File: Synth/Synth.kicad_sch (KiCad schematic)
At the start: 13 parts, among them SW1 Reset, SW2 Boot, U1 ESP32-S2-SOLO, U11 LM321, U12 LM321, U2 LM321

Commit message: changed the potentiometer footprints
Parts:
- C10, C7, C8, C9: footprint (none) -> Capacitor_SMD:C_0805_2012Metric
- R1, R2, R3: footprint (none) -> Resistor_SMD:R_0805_2012Metric
- SW1: footprint (none) -> Button_Switch_SMD:SW_DIP_SPSTx01_Slide_6.7x4.1mm_W6.73mm_P2.54mm_LowProfile_JPin
- SW2: footprint (none) -> Button_Switch_THT:SW_PUSH_6mm_H7.3mm
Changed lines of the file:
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@@
       (effects (font (size 1.27 1.27)) (justify left))
     )
-    (property "Footprint" "" (at 194.6402 30.353 0)
+    (property "Footprint" "Capacitor_SMD:C_0805_2012Metric" (at 194.6402 30.353 0)
       (effects (font (size 1.27 1.27)) hide)
     )
@@
       (effects (font (size 1.27 1.27)) (justify left))
     )
-    (property "Footprint" "" (at 147.447 40.767 0)
+    (property "Footprint" "Resistor_SMD:R_0805_2012Metric" (at 147.447 40.767 0)
       (effects (font (size 1.27 1.27)) hide)
     )
@@
       (effects (font (size 1.27 1.27)))
     )
-    (property "Footprint" "" (at 255.143 71.7042 0)
+    (property "Footprint" "Capacitor_SMD:C_0805_2012Metric" (at 255.143 71.7042 0)
       (effects (font (size 1.27 1.27)) hide)
     )
@@
       (effects (font (size 1.27 1.27)))
     )
-    (property "Footprint" "" (at 138.049 37.846 0)
+    (property "Footprint" "Button_Switch_SMD:SW_DIP_SPSTx01_Slide_6.7x4.1mm_W6.73mm_P2.54mm_LowProfile_JPin" (at 138.049 37.846 0)
       (effects (font (size 1.27 1.27)) hide)
     )
@@
       (effects (font (size 1.27 1.27)))
     )
-    (property "Footprint" "" (at 272.288 85.344 0)
+    (property "Footprint" "Resistor_SMD:R_0805_2012Metric" (at 272.288 85.344 0)
       (effects (font (size 1.27 1.27)) hide)
     )
@@
       (effects (font (size 1.27 1.27)))
     )
-    (property "Footprint" "" (at 258.318 57.023 0)
+    (property "Footprint" "Button_Switch_THT:SW_PUSH_6mm_H7.3mm" (at 258.318 57.023 0)
       (effects (font (size 1.27 1.27)) hide)
     )
@@
       (effects (font (size 1.27 1.27)) (justify left))
     )
-    (property "Footprint" "" (at 255.397 89.535 0)
+    (property "Footprint" "Resistor_SMD:R_0805_2012Metric" (at 255.397 89.535 0)
       (effects (font (size 1.27 1.27)) hide)
     )
@@
       (effects (font (size 1.27 1.27)))
     )
-    (property "Footprint" "" (at 134.112 50.3682 0)
+    (property "Footprint" "Capacitor_SMD:C_0805_2012Metric" (at 134.112 50.3682 0)
       (effects (font (size 1.27 1.27)) hide)
     )
@@
       (effects (font (size 1.27 1.27)) (justify left))
     )
-    (property "Footprint" "" (at 202.6412 30.353 0)
-      (effects (font (size 1.27 1.27)) hide)
-    )
+    (property "Footprint" "Capacitor_SMD:C_0805_2012Metric" (at 202.6412 30.353 0)
+      (effects (font (size 1.27 1.27)) hide)
+    )

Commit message: almost done w layoutgit add *
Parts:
- added JP1+1: SolderJumper_2_Open, Jumper:SolderJumper-2_P1.3mm_Bridged_RoundedPad1.0x1.5mm, symbol Jumper:SolderJumper_2_Open
- added R4: 20k, Resistor_SMD:R_0805_2012Metric, symbol Device:R
- added RV1: 20k, Potentiometer_THT:Potentiometer_Bourns_3299W_Vertical, symbol Device:R_Potentiometer
- added TP1: TestPoint, TestPoint:TestPoint_Pad_2.5x2.5mm, symbol Connector:TestPoint
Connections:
- net GND: now also R4.2, TP1.1
- net V_out+: now also RV1.1
- new net: JP1+1.1 (A), RV1.2, RV1.3
- new net: JP1+1.2 (B), R4.1
- no-connect marks 0 -> 34

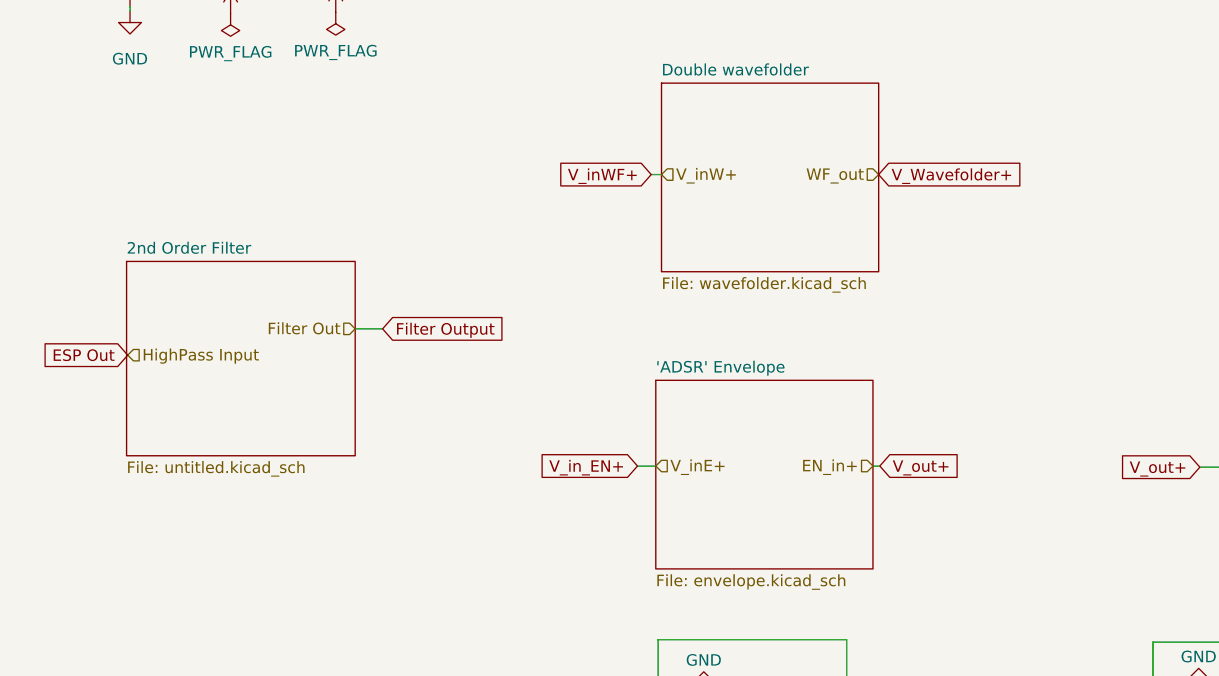
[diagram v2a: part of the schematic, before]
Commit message: changed hierarchical labels
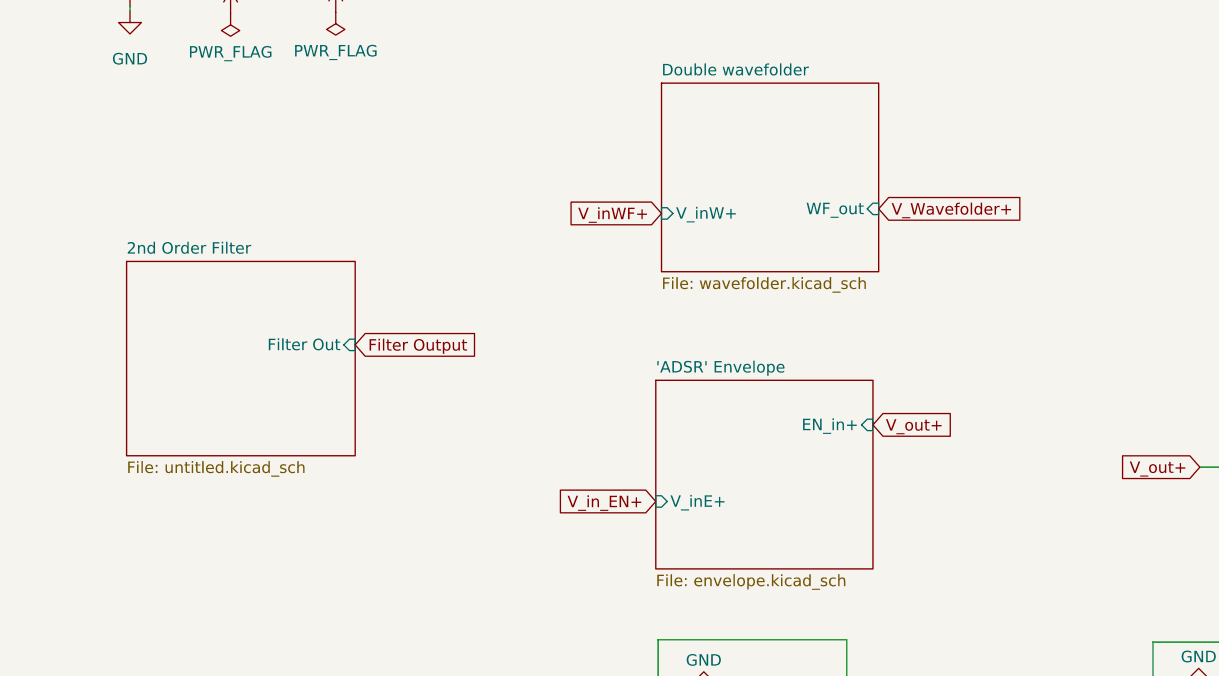
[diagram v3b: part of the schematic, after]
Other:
- sheet 'ADSR' Envelope ports: added EN_in+, V_inE+; removed none
- sheet 2nd Order Filter ports: added Filter Out; removed none
- sheet Double wavefolder ports: added V_inW+, WF_out; removed none
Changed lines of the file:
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@@
-    (stroke (width 0) (type default))
-  )
-  (wire (pts (xy 80.137 146.177) (xy 82.169 146.177))
     (stroke (width 0) (type default))
   )
@@
     (stroke (width 0) (type default))
   )
-  (wire (pts (xy 51.816 130.937) (xy 48.768 130.937))
-    (stroke (width 0) (type default))
-  )
   (wire (pts (xy 255.397 84.963) (xy 262.636 84.963))
     (stroke (width 0) (type default))
   )
-  (wire (pts (xy 81.661 113.792) (xy 82.804 113.792))
-    (stroke (width 0) (type default))
-  )
   (wire (pts (xy 103.378 179.197) (xy 104.648 179.197))
     (stroke (width 0) (type default))
   )
-  (wire (pts (xy 107.061 146.177) (xy 106.299 146.177))
-    (stroke (width 0) (type default))
-  )
   (wire (pts (xy 103.378 165.481) (xy 103.378 179.197))
     (stroke (width 0) (type default))
   )
-  (global_label "Filter Output" (shape input) (at 51.816 130.937 0) (fields_autoplaced)
-    (effects (font (size 1.27 1.27)) (justify left))
-    (property "Intersheetrefs" "${INTERSHEET_REFS}" (at 66.9568 130.937 0)
-      (effects (font (size 1.27 1.27)) (justify left) hide)
+  (global_label "V_inWF+" (shape input) (at 82.804 118.11 180) (fields_autoplaced)
+    (effects (font (size 1.27 1.27)) (justify right))
+    (property "Intersheetrefs" "${INTERSHEET_REFS}" (at 71.8964 118.11 0)
+      (effects (font (size 1.27 1.27)) (justify right) hide)
     )
   )
@@
     )
   )
-  (global_label "ESP Out" (shape input) (at 23.495 133.858 180) (fields_autoplaced)
-    (effects (font (size 1.27 1.27)) (justify right))
-    (property "Intersheetrefs" "${INTERSHEET_REFS}" (at 12.7085 133.858 0)
-      (effects (font (size 1.27 1.27)) (justify right) hide)
-    )
-  )
   (global_label "ESP Out" (shape input) (at 278.003 96.012 0) (fields_autoplaced)
     (effects (font (size 1.27 1.27)) (justify left))
@@
     )
   )
-  (global_label "V_Wavefolder+" (shape input) (at 106.934 113.792 0) (fields_autoplaced)
+  (global_label "V_Wavefolder+" (shape input) (at 106.934 117.602 0) (fields_autoplaced)
     (effects (font (size 1.27 1.27)) (justify left))
-    (property "Intersheetrefs" "${INTERSHEET_REFS}" (at 123.7681 113.792 0)
+    (property "Intersheetrefs" "${INTERSHEET_REFS}" (at 123.7681 117.602 0)
       (effects (font (size 1.27 1.27)) (justify left) hide)
     )
   )
-  (global_label "V_out+" (shape input) (at 107.061 146.177 0) (fields_autoplaced)
+  (global_label "Filter Output" (shape input) (at 48.768 132.715 0) (fields_autoplaced)
     (effects (font (size 1.27 1.27)) (justify left))
-    (property "Intersheetrefs" "${INTERSHEET_REFS}" (at 116.6985 146.177 0)
+    (property "Intersheetrefs" "${INTERSHEET_REFS}" (at 63.9088 132.715 0)
       (effects (font (size 1.27 1.27)) (justify left) hide)
     )
   )
-  (global_label "V_inWF+" (shape input) (at 81.661 113.792 180) (fields_autoplaced)
-    (effects (font (size 1.27 1.27)) (justify right))
-    (property "Intersheetrefs" "${INTERSHEET_REFS}" (at 70.7534 113.792 0)
-      (effects (font (size 1.27 1.27)) (justify right) hide)
+  (global_label "V_out+" (shape input) (at 106.299 141.605 0) (fields_autoplaced)
+    (effects (font (size 1.27 1.27)) (justify left))
+    (property "Intersheetrefs" "${INTERSHEET_REFS}" (at 115.9365 141.605 0)
+      (effects (font (size 1.27 1.27)) (justify left) hide)
     )
   )
@@
     )
   )
-  (global_label "V_in_EN+" (shape input) (at 80.137 146.177 180) (fields_autoplaced)
+  (global_label "V_in_EN+" (shape input) (at 82.169 150.114 180) (fields_autoplaced)
     (effects (font (size 1.27 1.27)) (justify right))
-    (property "Intersheetrefs" "${INTERSHEET_REFS}" (at 68.3223 146.177 0)
+    (property "Intersheetrefs" "${INTERSHEET_REFS}" (at 70.3543 150.114 0)
       (effects (font (size 1.27 1.27)) (justify right) hide)
     )
-  )
-  (hierarchical_label "WF_out" (shape input) (at 106.934 113.792 180) (fields_autoplaced)
-    (effects (font (size 1.27 1.27)) (justify right))
-  )
-  (hierarchical_label "V_inE+" (shape input) (at 82.169 146.177 0) (fields_autoplaced)
-    (effects (font (size 1.27 1.27)) (justify left))
-  )
-  (hierarchical_label "V_inW+" (shape input) (at 82.804 113.792 0) (fields_autoplaced)
-    (effects (font (size 1.27 1.27)) (justify left))
-  )
-  (hierarchical_label "HighPass Input" (shape input) (at 23.495 133.858 0) (fields_autoplaced)
-    (effects (font (size 1.27 1.27)) (justify left))
-  )
-  (hierarchical_label "EN_in+" (shape input) (at 106.299 146.177 180) (fields_autoplaced)
-    (effects (font (size 1.27 1.27)) (justify right))
-  )
-  (hierarchical_label "Filter Out" (shape input) (at 48.768 130.937 180) (fields_autoplaced)
-    (effects (font (size 1.27 1.27)) (justify right))
   )
   (symbol (lib_id "power:GND") (at 23.749 95.631 0) (unit 1)
@@
       (effects (font (size 1.27 1.27)) (justify left top))
     )
+    (pin "Filter Out" input (at 48.768 132.715 0)
+      (effects (font (size 1.27 1.27)) (justify right))
+    )
     (instances
       (project "Synth"
@@
       (effects (font (size 1.27 1.27)) (justify left top))
     )
+    (pin "EN_in+" input (at 106.299 141.605 0)
+      (effects (font (size 1.27 1.27)) (justify right))
+    )
+    (pin "V_inE+" input (at 82.169 150.114 180)
+      (effects (font (size 1.27 1.27)) (justify left))
+    )
     (instances
       (project "Synth"
@@
       (effects (font (size 1.27 1.27)) (justify left top))
     )
-    (instances
+    (pin "V_inW+" input (at 82.804 118.11 180)
+      (effects (font (size 1.27 1.27)) (justify left))
+    )
+    (pin "WF_out" input (at 106.934 117.602 0)
+      (effects (font (size 1.27 1.27)) (justify right))
+    )
+    (instances

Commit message: fixed
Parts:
- added TP2, TP3, TP4, TP5, TP6, TP7: TestPoint, TestPoint:TestPoint_Pad_2.5x2.5mm, symbol Connector:TestPoint
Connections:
- net +12V: now also TP7.1
- net +3.3V: now also TP6.1
- net Filter Output: now also TP2.1
- net V_Envelope+: now also TP5.1
- net V_Wavefolder+: now also TP4.1
- net V_out+: now also TP3.1
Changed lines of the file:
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@@
     (stroke (width 0) (type default))
+  )
+  (global_label "V_out+" (shape input) (at 64.77 75.311 90) (fields_autoplaced)
+    (effects (font (size 1.27 1.27)) (justify left))
+    (property "Intersheetrefs" "${INTERSHEET_REFS}" (at 64.77 65.6735 90)
+      (effects (font (size 1.27 1.27)) (justify left) hide)
+    )
   )
   (global_label "V_inWF+" (shape input) (at 82.804 118.11 180) (fields_autoplaced)
@@
     )
   )
+  (global_label "Filter Output" (shape input) (at 73.787 77.851 270) (fields_autoplaced)
+    (effects (font (size 1.27 1.27)) (justify right))
+    (property "Intersheetrefs" "${INTERSHEET_REFS}" (at 73.787 92.9918 90)
+      (effects (font (size 1.27 1.27)) (justify right) hide)
+    )
+  )
   (global_label "Filter Output" (shape input) (at 48.768 132.715 0) (fields_autoplaced)
     (effects (font (size 1.27 1.27)) (justify left))
@@
     )
   )
+  (global_label "V_Envelope+" (shape input) (at 64.77 57.15 90) (fields_autoplaced)
+    (effects (font (size 1.27 1.27)) (justify left))
+    (property "Intersheetrefs" "${INTERSHEET_REFS}" (at 64.77 42.1302 90)
+      (effects (font (size 1.27 1.27)) (justify left) hide)
+    )
+  )
   (global_label "V_out+" (shape input) (at 106.299 141.605 0) (fields_autoplaced)
     (effects (font (size 1.27 1.27)) (justify left))
@@
     )
   )
+  (global_label "V_Wavefolder+" (shape input) (at 73.406 57.658 90) (fields_autoplaced)
+    (effects (font (size 1.27 1.27)) (justify left))
+    (property "Intersheetrefs" "${INTERSHEET_REFS}" (at 73.406 40.8239 90)
+      (effects (font (size 1.27 1.27)) (justify left) hide)
+    )
+  )
   (global_label "V_in_EN+" (shape input) (at 82.169 150.114 180) (fields_autoplaced)
     (effects (font (size 1.27 1.27)) (justify right))
@@
         (path "/69caad27-d98a-4cdc-abd0-794bd5e6ba79"
           (reference "U2") (unit 1)
+        )
+      )
+    )
+  )
+  (symbol (lib_id "power:+3.3V") (at 88.138 67.056 0) (unit 1)
+    (in_bom yes) (on_board yes) (dnp no) (fields_autoplaced)
+    (property "Reference" "#PWR050" (at 88.138 70.866 0)
+      (effects (font (size 1.27 1.27)) hide)
+    )
+    (property "Value" "+3.3V" (at 88.138 62.357 0)
+      (effects (font (size 1.27 1.27)))
+    )
+    (property "Footprint" "" (at 88.138 67.056 0)
+      (effects (font (size 1.27 1.27)) hide)
+    )
+    (property "Datasheet" "" (at 88.138 67.056 0)
+      (effects (font (size 1.27 1.27)) hide)
+    )
+    (pin "1")
+    (instances
+      (project "Synth"
+        (path "/69caad27-d98a-4cdc-abd0-794bd5e6ba79"
+          (reference "#PWR050") (unit 1)
         )
       )
@@
     )
   )
+  (symbol (lib_id "Connector:TestPoint") (at 64.77 57.15 180) (unit 1)
+    (in_bom yes) (on_board yes) (dnp no) (fields_autoplaced)
+    (property "Reference" "TP5" (at 66.294 59.182 0)
+      (effects (font (size 1.27 1.27)) (justify right))
+    )
+    (property "Value" "TestPoint" (at 66.294 61.722 0)
+      (effects (font (size 1.27 1.27)) (justify right))
+    )
+    (property "Footprint" "TestPoint:TestPoint_Pad_2.5x2.5mm" (at 59.69 57.15 0)
+      (effects (font (size 1.27 1.27)) hide)
+    )
+    (property "Datasheet" "~" (at 59.69 57.15 0)
+      (effects (font (size 1.27 1.27)) hide)
+    )
+    (pin "1")
+    (instances
+      (project "Synth"
+        (path "/69caad27-d98a-4cdc-abd0-794bd5e6ba79"
+          (reference "TP5") (unit 1)
+        )
+      )
+    )
+  )
   (symbol (lib_id "power:GND") (at 87.503 171.577 180) (unit 1)
     (in_bom yes) (on_board yes) (dnp no)
@@
     )
   )
+  (symbol (lib_id "Connector:TestPoint") (at 73.406 57.658 180) (unit 1)
+    (in_bom yes) (on_board yes) (dnp no) (fields_autoplaced)
+    (property "Reference" "TP4" (at 74.93 59.69 0)
+      (effects (font (size 1.27 1.27)) (justify right))
+    )
+    (property "Value" "TestPoint" (at 74.93 62.23 0)
+      (effects (font (size 1.27 1.27)) (justify right))
+    )
+    (property "Footprint" "TestPoint:TestPoint_Pad_2.5x2.5mm" (at 68.326 57.658 0)
+      (effects (font (size 1.27 1.27)) hide)
+    )
+    (property "Datasheet" "~" (at 68.326 57.658 0)
+      (effects (font (size 1.27 1.27)) hide)
+    )
+    (pin "1")
+    (instances
+      (project "Synth"
+        (path "/69caad27-d98a-4cdc-abd0-794bd5e6ba79"
+          (reference "TP4") (unit 1)
+        )
+      )
+    )
+  )
   (symbol (lib_id "power:PWR_FLAG") (at 33.655 78.994 180) (unit 1)
     (in_bom yes) (on_board yes) (dnp no) (fields_autoplaced)
@@
         (path "/69caad27-d98a-4cdc-abd0-794bd5e6ba79"
           (reference "#PWR048") (unit 1)
+        )
+      )
+    )
+  )
+  (symbol (lib_id "Connector:TestPoint") (at 73.787 77.851 0) (unit 1)
+    (in_bom yes) (on_board yes) (dnp no) (fields_autoplaced)
+    (property "Reference" "TP2" (at 76.2 73.279 0)
+      (effects (font (size 1.27 1.27)) (justify left))
+    )
+    (property "Value" "TestPoint" (at 76.2 75.819 0)
+      (effects (font (size 1.27 1.27)) (justify left))
+    )
+    (property "Footprint" "TestPoint:TestPoint_Pad_2.5x2.5mm" (at 78.867 77.851 0)
+      (effects (font (size 1.27 1.27)) hide)
+    )
+    (property "Datasheet" "~" (at 78.867 77.851 0)
+      (effects (font (size 1.27 1.27)) hide)
+    )
+    (pin "1")
+    (instances
+      (project "Synth"
+        (path "/69caad27-d98a-4cdc-abd0-794bd5e6ba79"
+          (reference "TP2") (unit 1)
         )
       )
@@
     )
   )
+  (symbol (lib_id "power:+12V") (at 98.425 67.056 0) (unit 1)
+    (in_bom yes) (on_board yes) (dnp no)
+    (property "Reference" "#PWR051" (at 98.425 70.866 0)
+      (effects (font (size 1.27 1.27)) hide)
+    )
+    (property "Value" "+12V" (at 98.425 62.611 0)
+      (effects (font (size 1.27 1.27)))
+    )
+    (property "Footprint" "" (at 98.425 67.056 0)
+      (effects (font (size 1.27 1.27)) hide)
+    )
+    (property "Datasheet" "" (at 98.425 67.056 0)
+      (effects (font (size 1.27 1.27)) hide)
+    )
+    (pin "1")
+    (instances
+      (project "Synth"
+        (path "/69caad27-d98a-4cdc-abd0-794bd5e6ba79"
+          (reference "#PWR051") (unit 1)
+        )
+      )
+    )
+  )
   (symbol (lib_id "Device:R_Small") (at 147.447 40.767 0) (unit 1)
     (in_bom yes) (on_board yes) (dnp no) (fields_autoplaced)
@@
         (path "/69caad27-d98a-4cdc-abd0-794bd5e6ba79"
           (reference "R3") (unit 1)
+        )
+      )
+    )
+  )
+  (symbol (lib_id "Connector:TestPoint") (at 64.77 75.311 180) (unit 1)
+    (in_bom yes) (on_board yes) (dnp no) (fields_autoplaced)
+    (property "Reference" "TP3" (at 67.31 77.343 0)
+      (effects (font (size 1.27 1.27)) (justify right))
+    )
+    (property "Value" "TestPoint" (at 67.31 79.883 0)
+      (effects (font (size 1.27 1.27)) (justify right))
+    )
+    (property "Footprint" "TestPoint:TestPoint_Pad_2.5x2.5mm" (at 59.69 75.311 0)
+      (effects (font (size 1.27 1.27)) hide)
+    )
+    (property "Datasheet" "~" (at 59.69 75.311 0)
+      (effects (font (size 1.27 1.27)) hide)
+    )
+    (pin "1")
+    (instances
+      (project "Synth"
+        (path "/69caad27-d98a-4cdc-abd0-794bd5e6ba79"
+          (reference "TP3") (unit 1)
         )
       )
@@
     )
   )
+  (symbol (lib_id "Connector:TestPoint") (at 98.425 67.056 180) (unit 1)
+    (in_bom yes) (on_board yes) (dnp no) (fields_autoplaced)
+    (property "Reference" "TP7" (at 99.949 69.088 0)
+      (effects (font (size 1.27 1.27)) (justify right))
+    )
+    (property "Value" "TestPoint" (at 99.949 71.628 0)
+      (effects (font (size 1.27 1.27)) (justify right))
+    )
+    (property "Footprint" "TestPoint:TestPoint_Pad_2.5x2.5mm" (at 93.345 67.056 0)
+      (effects (font (size 1.27 1.27)) hide)
+    )
+    (property "Datasheet" "~" (at 93.345 67.056 0)
+      (effects (font (size 1.27 1.27)) hide)
+    )
+    (pin "1")
+    (instances
+      (project "Synth"
+        (path "/69caad27-d98a-4cdc-abd0-794bd5e6ba79"
+          (reference "TP7") (unit 1)
+        )
+      )
+    )
+  )
   (symbol (lib_id "Device:C") (at 201.676 26.543 0) (unit 1)
     (in_bom yes) (on_board yes) (dnp no) (fields_autoplaced)
@@
         )
       )
+    )
+  )
+  (symbol (lib_id "Connector:TestPoint") (at 88.138 67.056 180) (unit 1)
+    (in_bom yes) (on_board yes) (dnp no) (fields_autoplaced)
+    (property "Reference" "TP6" (at 89.662 69.088 0)
+      (effects (font (size 1.27 1.27)) (justify right))
+    )
+    (property "Value" "TestPoint" (at 89.662 71.628 0)
+      (effects (font (size 1.27 1.27)) (justify right))
+    )
+    (property "Footprint" "TestPoint:TestPoint_Pad_2.5x2.5mm" (at 83.058 67.056 0)
+      (effects (font (size 1.27 1.27)) hide)
+    )
+    (property "Datasheet" "~" (at 83.058 67.056 0)
+      (effects (font (size 1.27 1.27)) hide)
+    )
+    (pin "1")
+    (instances
+      (project "Synth"
+        (path "/69caad27-d98a-4cdc-abd0-794bd5e6ba79"
+          (reference "TP6") (unit 1)
+        )
+      )
